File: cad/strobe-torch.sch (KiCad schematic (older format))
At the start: 29 parts, among them SW1 50Hz, SW2 60Hz, SW3 300Hz, U1 ATTINY25V-10SU, Y1 4.9152MHz

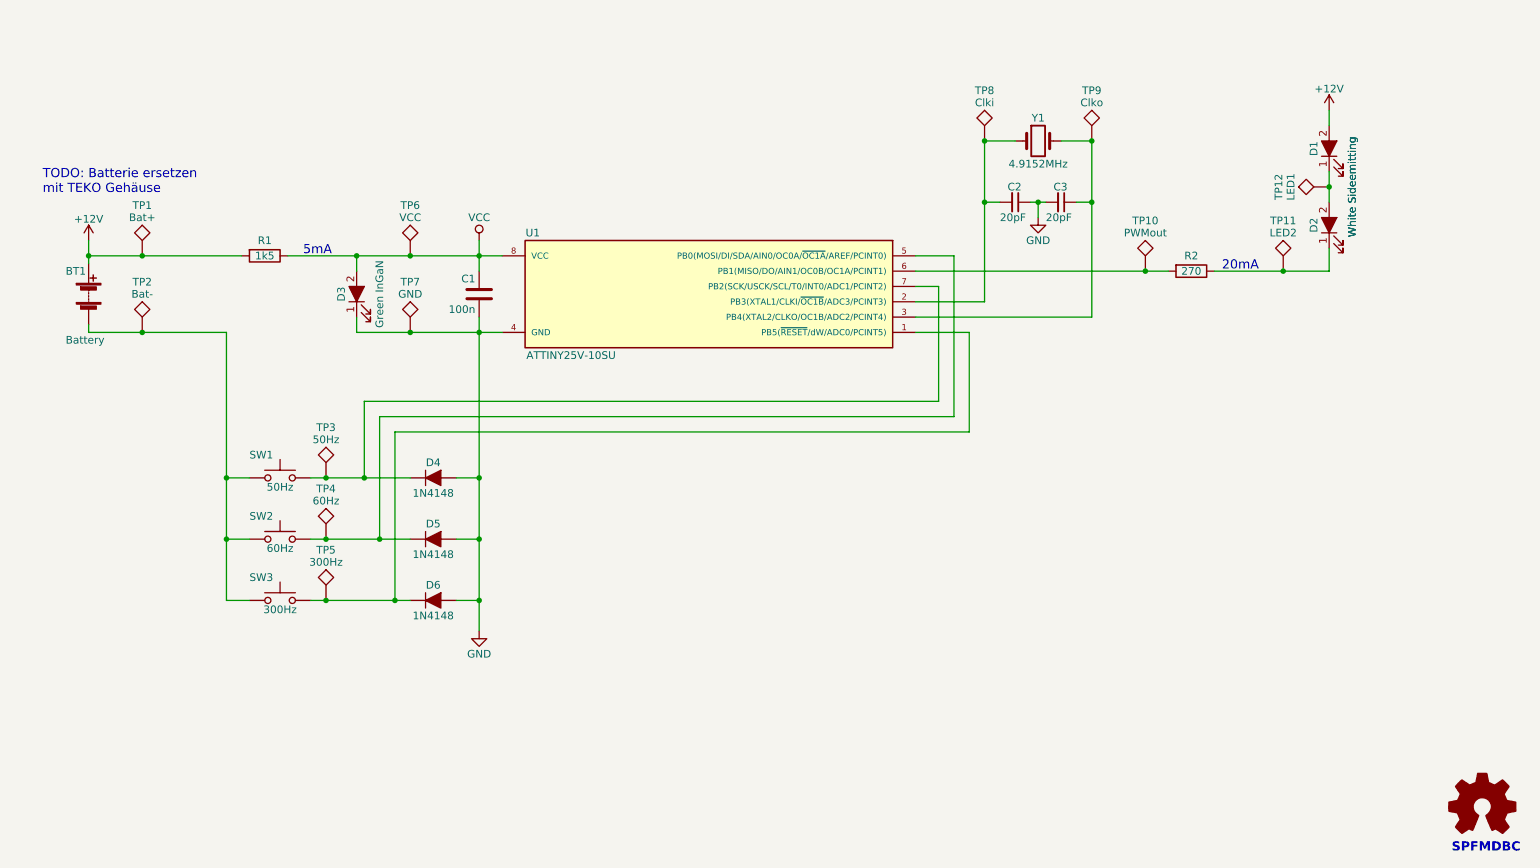
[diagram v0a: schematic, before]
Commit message: Updated schematic (Output MOSFET and change to Shottky diodes, changed pinning to optimize layout)
Created footprints for Teko case and side emitting LEDs

Initial pcb layout
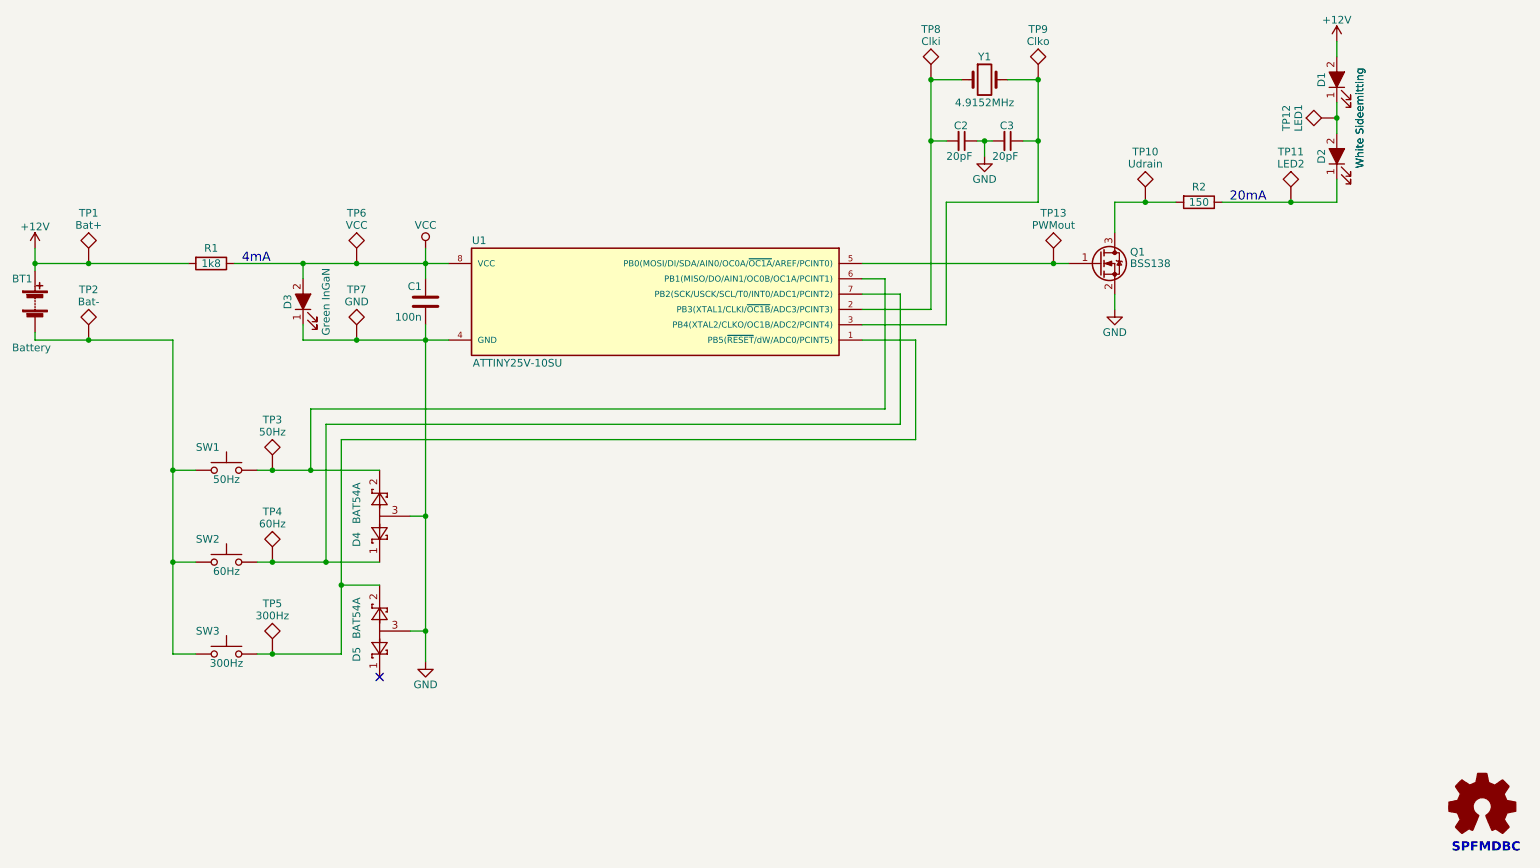
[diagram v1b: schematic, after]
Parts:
- removed D4, D5, D6: 1N4148, Diodes_SMD:D_MiniMELF, symbol D_ALT
- added D4, D5: BAT54A, TO_SOT_Packages_SMD:SOT-23, symbol BAT54A
- added Q1: BSS138, TO_SOT_Packages_SMD:SOT-23, symbol BSS138
- added TP13: PWMout, Measurement_Points:Measurement_Point_Round-SMD-Pad_Small, symbol TEST
- BT1: footprint Pin_Headers:Pin_Header_Straight_1x02_Pitch2.54mm -> Battery_Holder:Teko_1112x_battery_compartment
- D1, D2: footprint LEDs:LED_1206 -> LEDs_Side_Emitting:LED_215
- R1: value 1k5 -> 1k8
- R2: value 270 -> 150
- SW1, SW2, SW3: footprint Buttons_Switches_SMD:SW_SPST_EVQP2 -> Buttons_Switches_SMD:SW_SPST_PTS645
- TP10: value PWMout -> Udrain
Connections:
- net GND: now also D4.3, D5.3, Q1.2 (S)
- net at SW3.2, TP5.1, U1.1 (PB5(~RESET~/dW/ADC0/PCINT5)): now also D5.2
- net at SW2.2, TP4.1: now also U1.7 (PB2(SCK/USCK/SCL/T0/INT0/ADC1/PCINT2)), D4.1; no longer U1.5 (PB0(MOSI/DI/SDA/AIN0/OC0A/~OC1A~/AREF/PCINT0))
- net at R2.2, TP10.1: now also Q1.3 (D); no longer U1.6 (PB1(MISO/DO/AIN1/OC0B/OC1A/PCINT1))
- net at SW1.2, TP3.1: now also U1.6 (PB1(MISO/DO/AIN1/OC0B/OC1A/PCINT1)), D4.2; no longer U1.7 (PB2(SCK/USCK/SCL/T0/INT0/ADC1/PCINT2))
- new net: Q1.1 (G), TP13.1, U1.5 (PB0(MOSI/DI/SDA/AIN0/OC0A/~OC1A~/AREF/PCINT0))
- no-connect marks 0 -> 1
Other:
- note added: "4mA"
- note removed: "5mA"
- note removed: "TODO: Batterie ersetzen\nmit TEKO Gehäuse"
- moved on the sheet: BT1, C1, C2, C3, D1, D2, D3, R1, R2, SW1, SW2, SW3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

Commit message: Applied needed modifications after production of first samples.
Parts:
- U1: footprint Housings_SOIC:SOIC-8_3.9x4.9mm_Pitch1.27mm -> Housings_SOIC:SO-8_5.3x6.2mm_Pitch1.27mm
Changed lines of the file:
@@
 F 0 "U1" H 6700 3900 50  0000 C CNN
 F 1 "ATTINY25V-10SU" H 6450 3100 50  0000 C CNN
-F 2 "Housings_SOIC:SOIC-8_3.9x4.9mm_Pitch1.27mm" H 6500 3500 50  0001 C CIN
+F 2 "Housings_SOIC:SO-8_5.3x6.2mm_Pitch1.27mm" H 6500 3500 50  0001 C CIN
 F 3 "" H 5550 3500 50  0001 C CNN
 F 4 "Microchip" H 5550 3500 60  0001 C CNN "Manufacturer"
